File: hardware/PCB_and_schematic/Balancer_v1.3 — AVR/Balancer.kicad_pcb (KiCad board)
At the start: 2 copper layers, 99.5 x 99.5 mm, 218 parts, among them J1 External Current Shunt, J10 BATT_12V, J11 LOAD_RESISTOR, J12 V_MEAS, J13 LED, J14 ICP, J15 RS485, J16 RS485, J17 Conn_01x01, J2 BATT_IN, J3 BATT_OUT, J4 TMP_BALANCER, J5 TMP_SMPS, J6 THERMISTOR_BATT, J7 LOAD_RESISTOR, J8 FAN_BALANCER, J9 FAN_SMPS, Q1 IRF540N, Q10 BC817, Q11 BC807, Q12 IRF540N, Q13 BC817, Q14 BC817, Q15 AO3400A, Q16 AO3400A, Q17 BC817, Q18 BC817, Q19 BC807, Q20 IRF540N, Q21 BC817, Q5 IRF4905, Q6 BC817, Q7 BC807, Q8 BC817, Q9 BC817, U1 74AHCT125, U10 B0505S-1W, U11 ST485, U12 INA226, U13 FAN7382, U14 NE555D, U2 LM324, U3 LMV358, U4 AVR64DD28, U5 LM317_TO-220, U6 LM7805_TO220, U7 TL432DBZ, U8 ADUM3211ARZ, U9 PC817

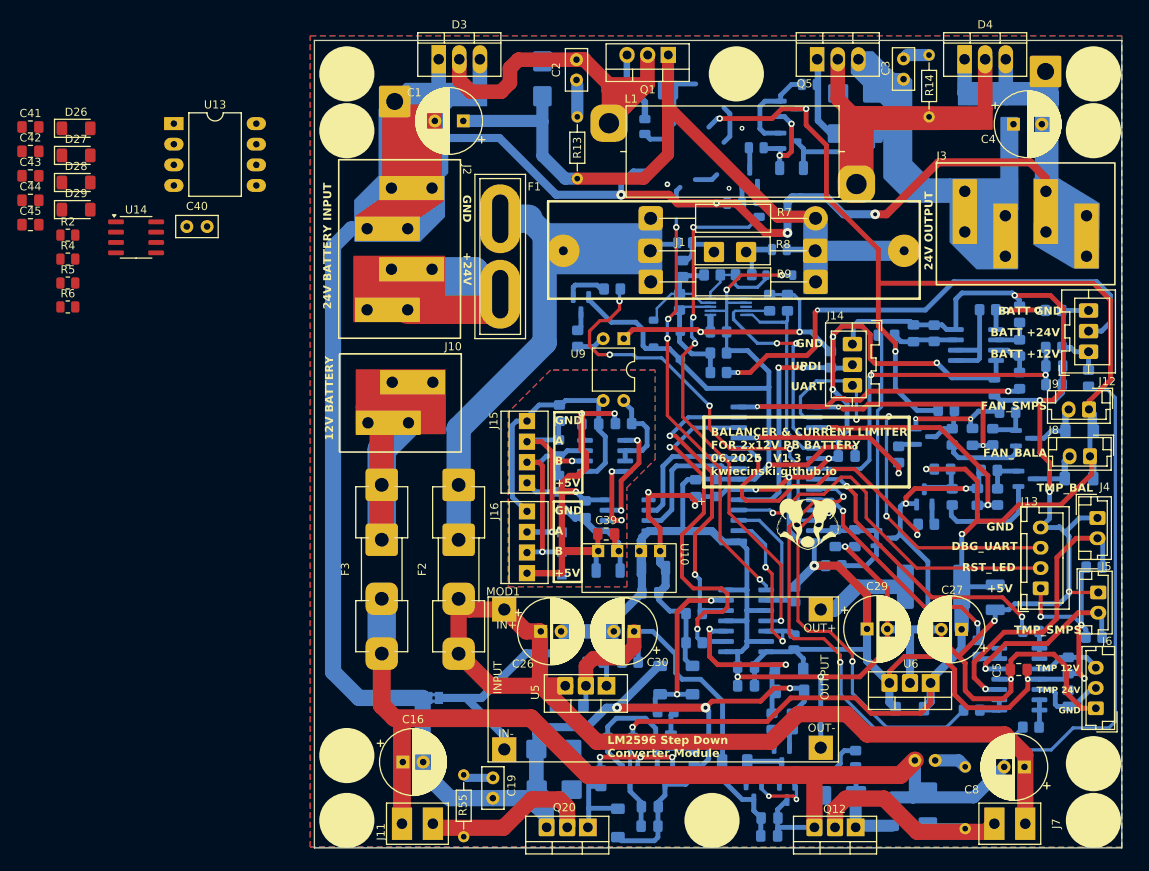
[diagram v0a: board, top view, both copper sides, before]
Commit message: add bms pcb balacer and smps separated
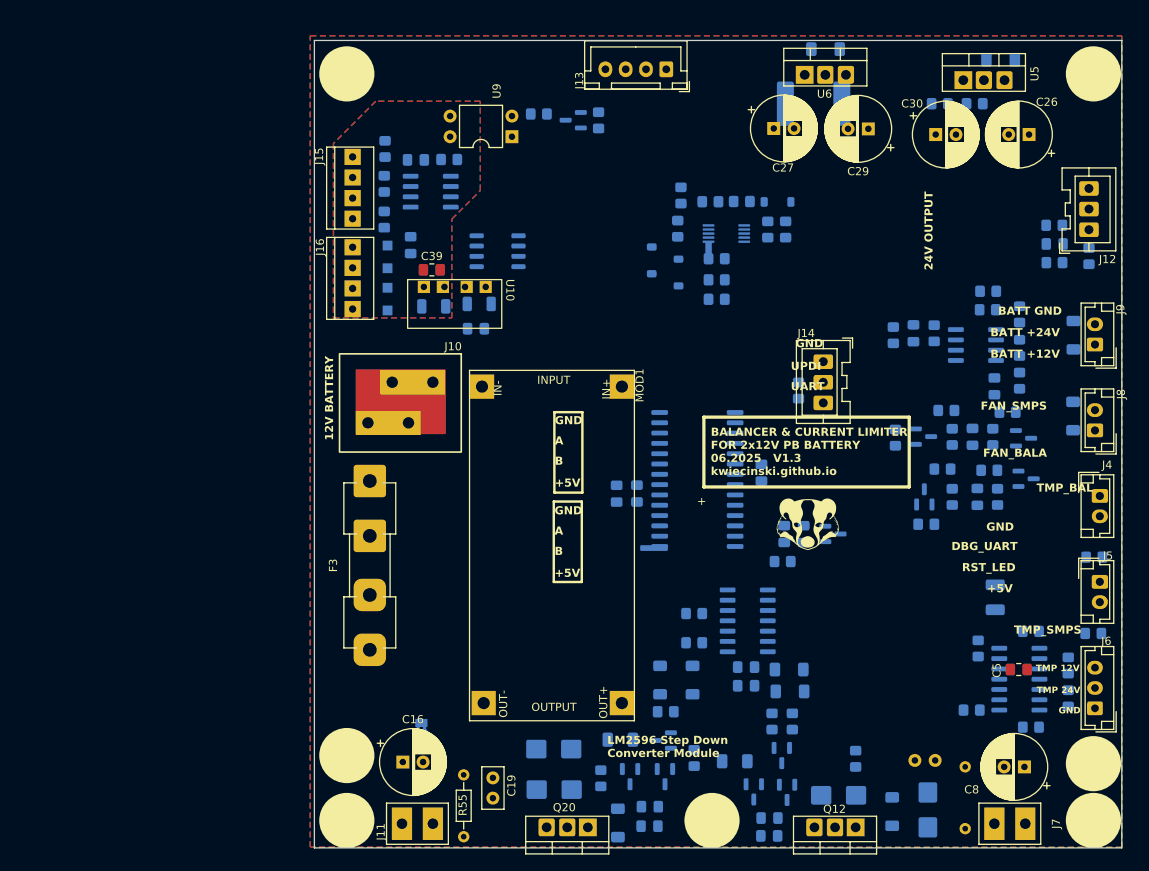
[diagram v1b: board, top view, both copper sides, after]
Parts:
- removed C1, C4: 100u/35V, Capacitor_THT:CP_Radial_D8.0mm_P3.50mm
- removed C2, C3: 1u, Capacitor_THT:C_Disc_D5.0mm_W2.5mm_P2.50mm
- removed C40: 100n, Capacitor_THT:C_Disc_D5.0mm_W2.5mm_P2.50mm
- removed C41, C42: 100n, Capacitor_SMD:C_0805_2012Metric_Pad1.18x1.45mm_HandSolder
- removed C43, C45: 10n, Capacitor_SMD:C_0805_2012Metric_Pad1.18x1.45mm_HandSolder
- removed C44: 1n, Capacitor_SMD:C_0805_2012Metric_Pad1.18x1.45mm_HandSolder
- removed D1, D2, D5, D6: SM6T15A, Diode_SMD:D_SMB
- removed D26, D28, D29: LL4148, Diode_SMD:D_MiniMELF
- removed D27: BZV55B15, Diode_SMD:D_MiniMELF
- removed D3, D4: YM3045, My-Footprints:TO-220-3_V_Thick_Pads
- removed F1: 6,3A, My-Footprints:Fuse_Blade_ATO_directSolder
- removed F2: 2A, My-Footprints:Fuseholder_Clip-5x20mm_Eaton_1A5601-01_Inline_P20.80x6.76mm_D1.70mm_Horizontal
- removed H2, H6, H8: MountingHole, My-Footprints:Mount-Hole-3mm
- removed J1: External Current Shunt, Connector_Hirose:Hirose_DF63M-2P-3.96DSA_1x02_P3.96mm_Vertical
- removed J17: Conn_01x01, Connector_Wire:SolderWire-1.5sqmm_1x01_D1.7mm_OD3.9mm
- removed J18: ~, Connector_Wire:SolderWire-1.5sqmm_1x01_D1.7mm_OD3.9mm
- removed J2: BATT_IN, My-Footprints-connectors:Flat-6,3mm-connector-4P
- removed J3: BATT_OUT, My-Footprints-connectors:Flat-6,3mm-connector-4P
- removed L1: L, My-Footprints:Inductor_Toroidal
- removed Q1: IRF540N, Package_TO_SOT_THT:TO-220-3_Vertical
- removed Q5: IRF4905, My-Footprints:TO-220-3_V_Thick_Pads
- removed Q6, Q8: BC817, Package_TO_SOT_SMD:SOT-23
- removed Q7: BC807, Package_TO_SOT_SMD:SOT-23
- removed R1, R2, R20: 10k, Resistor_SMD:R_0805_2012Metric
- removed R10: 20A/75mV, My-Footprints:Resistor-Power-5W-L22-W10
- removed R11, R3: 0R, Resistor_SMD:R_0805_2012Metric
- removed R12, R15, R4: 10R, Resistor_SMD:R_0805_2012Metric
- removed R13, R14: 10R, Resistor_THT:R_Axial_DIN0204_L3.6mm_D1.6mm_P7.62mm_Horizontal
- removed R16: 10k, Resistor_SMD:R_1206_3216Metric
- removed R17, R19, R5: 1k, Resistor_SMD:R_0805_2012Metric
- removed R18: 100R, Resistor_SMD:R_0805_2012Metric
- removed R6: 100k, Resistor_SMD:R_0805_2012Metric
- removed R7, R8, R9: 20A/75mV, Resistor_THT:R_Axial_DIN0309_L9.0mm_D3.2mm_P20.32mm_Horizontal
- removed U13: FAN7382, Package_DIP:DIP-8_W10.16mm_LongPads
- removed U14: NE555D, Package_SO:SOIC-8_3.9x4.9mm_P1.27mm
- moved D19 95.7 mm to (241.6, 53.3), turned to 180 degrees
- moved U5 86.6 mm to (237.0, 55.8), turned to 0 degrees
- moved C26 85.8 mm to (245.1, 62.5), turned to 180 degrees
- moved R64 83.2 mm to (238.4, 58.7), turned to 0 degrees
- moved D20 81.9 mm to (220.0, 52.0), turned to 0 degrees
- moved J13 78.9 mm to (200.4, 54.4), turned to 180 degrees
- moved R62 78.7 mm to (234.1, 58.7), turned to 180 degrees
- moved U6 76.5 mm to (217.4, 55.1), turned to 0 degrees
- moved C30 71.6 mm to (233.6, 62.5), turned to 0 degrees
- moved C27 65.9 mm to (213.6, 61.7), turned to 0 degrees
- moved C29 61.6 mm to (225.3, 61.8), turned to 180 degrees
- moved F4 61.3 mm to (218.5, 58.7), turned to 180 degrees
- moved MOD1 48.3 mm to (176.1, 91.5), turned to 0 degrees
- moved C31 39.0 mm to (177.3, 83.3)
- moved C33 39.0 mm to (169.5, 65.6)
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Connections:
- U1 pad 11: Net-(R19-Pad1) -> (no net)
- U1 pad 12: PWM_OUT_CHRG -> (no net)
- U1 pad 13: GND -> (no net)
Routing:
- net GND: track 477.0 -> 0.00 mm, vias 20 -> 0
- net GNDA: track 350.8 -> 0.00 mm, vias 7 -> 0
- net +5V: track 263.3 -> 0.00 mm, vias 15 -> 0
- net +12V_LOCAL: track 233.1 -> 0.00 mm, vias 6 -> 0
- net +BATT_12V: track 200.7 -> 0.00 mm
- net +BATT_24V: track 127.6 -> 0.00 mm
- net Net-(D1-A1): track 98.1 -> 0.00 mm
- net Net-(D2-A2): track 70.6 -> 0.00 mm
- net Net-(J2-Pin_3): track 66.2 -> 0.00 mm
- net Net-(R19-Pad1): track 64.8 -> 0.00 mm, vias 4 -> 0
- net DC_LINE_24V: track 62.9 -> 0.00 mm
- net Net-(F1-Pad2): track 62.6 -> 0.00 mm
- net TEMP_AKU_24V: track 62.5 -> 0.00 mm, vias 2 -> 0
- net VOLTAGE_BATT_24V_3W: track 61.6 -> 0.00 mm, vias 2 -> 0
- net (no net): track 61.3 -> 0.00 mm, vias 4 -> 0
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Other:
- board text removed: "+24V"
- board text removed: "24V BATTERY INPUT"

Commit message: routing power module
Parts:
- added J1: batt-24V-balancer, Connector_PinSocket_2.54mm:PinSocket_1x04_P2.54mm_Vertical, F.Cu at (189.9, 63.1)
- added J2: pwm-12v-local, Connector_PinSocket_2.54mm:PinSocket_1x04_P2.54mm_Vertical, F.Cu at (194.5, 63.1)
- added J3: R-Shunt, Connector_PinHeader_2.54mm:PinHeader_1x02_P2.54mm_Vertical, F.Cu at (199.1, 63.1)
- C39: moved to B.Cu
- moved F4 79.3 mm to (187.4, 131.6)
- moved R65 8.02 mm to (184.7, 64.0), turned to 0 degrees
- moved D20 7.05 mm to (219.8, 59.0)
- moved J13 6.00 mm to (206.3, 55.3)
- moved D19 5.26 mm to (241.0, 58.5)
- moved C32 4.93 mm to (181.5, 84.6)
- moved C39 4.81 mm to (175.2, 82.2)
- moved Q21 4.40 mm to (184.5, 60.7), turned to 90 degrees
- moved C31 3.91 mm to (181.0, 82.2)
- moved U10 3.77 mm to (172.1, 79.1)
- moved D12 3.44 mm to (250.3, 93.7)
- moved D13 3.44 mm to (250.3, 83.8)
- moved J12 3.44 mm to (252.3, 70.8)
- moved J4 3.44 mm to (253.6, 103.6)
- moved J5 3.44 mm to (253.6, 114.2)
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
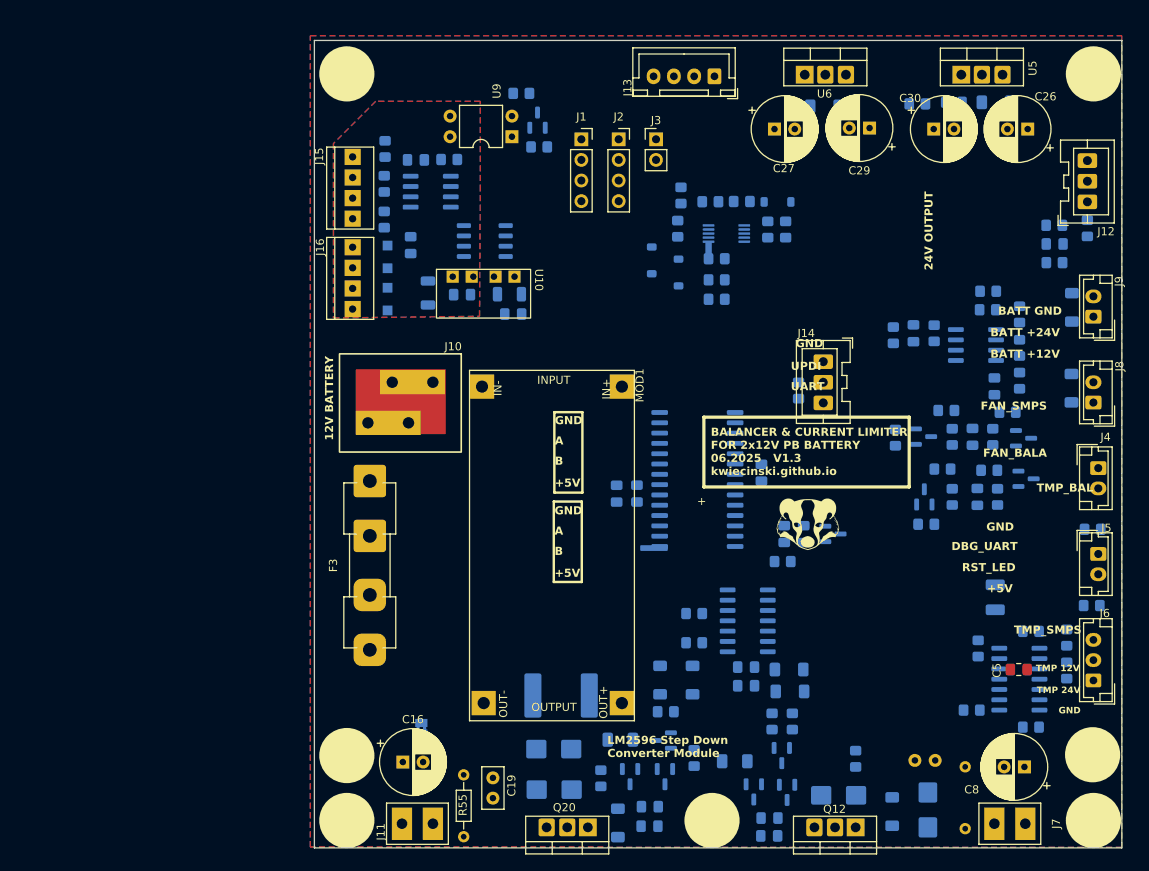
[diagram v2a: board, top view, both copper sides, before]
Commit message: done PCB power module and balancer
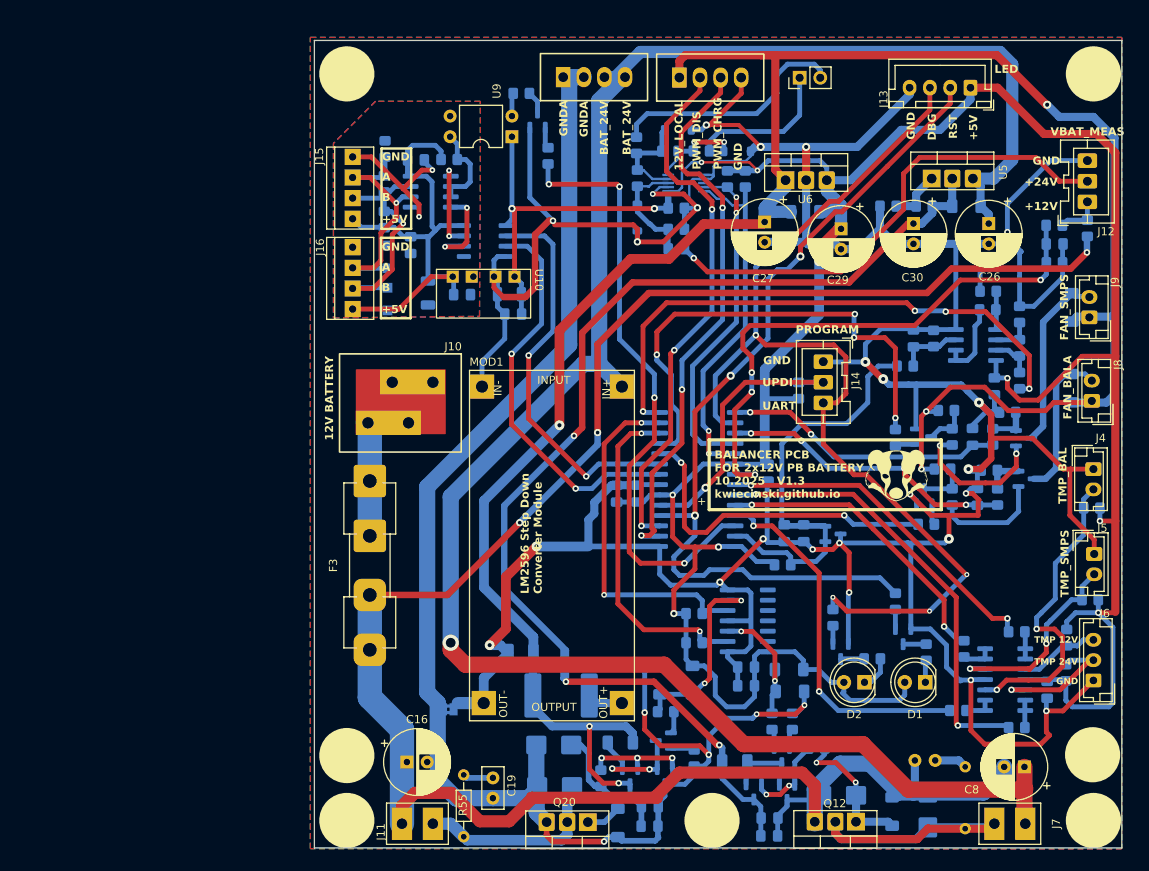
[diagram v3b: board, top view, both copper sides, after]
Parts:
- added D1: LED, LED_THT:LED_D5.0mm, F.Cu at (232.3, 130.0)
- added D2: LED, LED_THT:LED_D5.0mm, F.Cu at (224.8, 130.0)
- added Q1: BC817, Package_TO_SOT_SMD:SOT-23, B.Cu at (229.6, 124.3)
- added Q2: BC817, Package_TO_SOT_SMD:SOT-23, B.Cu at (221.8, 126.2)
- added R1: 10K, Resistor_SMD:R_0805_2012Metric_Pad1.20x1.40mm_HandSolder, B.Cu at (228.6, 120.0)
- added R2: 220R, Resistor_SMD:R_0805_2012Metric_Pad1.20x1.40mm_HandSolder, B.Cu at (232.4, 126.3)
- added R3: 10K, Resistor_SMD:R_0805_2012Metric_Pad1.20x1.40mm_HandSolder, B.Cu at (220.9, 122.0)
- added R4: 220R, Resistor_SMD:R_0805_2012Metric_Pad1.20x1.40mm_HandSolder, B.Cu at (225.8, 127.1)
- C5: moved to B.Cu
- J2: footprint Connector_PinSocket_2.54mm:PinSocket_1x04_P2.54mm_Vertical -> My-Footprints-connectors:PinSocket_1x04_P2.54mm_Vertical
- moved C24 58.9 mm to (182.5, 126.4), turned to 180 degrees
- moved J13 31.6 mm to (237.8, 56.7)
- moved J3 19.3 mm to (216.8, 55.5), turned to 90 degrees
- moved D24 16.4 mm to (201.8, 61.9), turned to 0 degrees
- moved U5 13.3 mm to (233.1, 67.9)
- moved D19 13.3 mm to (237.3, 71.3)
- moved R64 13.3 mm to (232.2, 71.3)
- moved D20 13.2 mm to (217.5, 72.0)
- moved U6 13.2 mm to (215.1, 68.1)
- moved R62 13.1 mm to (227.7, 71.3)
- moved C29 12.9 mm to (221.9, 74.1), turned to -90 degrees
- moved C26 12.6 mm to (240.1, 73.4), turned to -90 degrees
- moved G*** 12.4 mm to (228.7, 104.5)
- moved C30 11.9 mm to (230.8, 73.4), turned to -90 degrees
- moved C27 11.5 mm to (212.5, 73.2), turned to -90 degrees
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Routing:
- net GND: track 0.00 -> 526.2 mm, vias 0 -> 23
- net +5V: track 0.00 -> 383.5 mm, vias 0 -> 11
- net +12V_LOCAL: track 0.00 -> 288.6 mm, vias 0 -> 6
- net +BATT_12V: track 0.00 -> 258.3 mm, vias 0 -> 3
- net +BATT_24V: track 0.00 -> 254.3 mm, vias 0 -> 1
- net GNDA: track 0.00 -> 190.9 mm, vias 0 -> 5
- net +24V_LOCAL: track 0.00 -> 156.9 mm, vias 0 -> 3
- net DBG_UART: track 0.00 -> 125.4 mm, vias 0 -> 5
- net LED1_PF6_RST: track 0.00 -> 108.1 mm, vias 0 -> 3
- net RS485_OUTPUT_ENABLE: track 0.00 -> 75.0 mm, vias 0 -> 4
- net VOLTAGE_BATT_12V: track 0.00 -> 70.1 mm, vias 0 -> 4
- net GND_VOLTAGE_DROP_ADC: track 0.00 -> 69.4 mm, vias 0 -> 4
- net PWM_OUT_CHRG: track 0.00 -> 68.7 mm, vias 0 -> 3
- net PWM_OUT_DISCH: track 0.00 -> 66.2 mm, vias 0 -> 3
- net PWM_FAN_SMPS: track 0.00 -> 60.9 mm, vias 0 -> 4
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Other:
- board text added: "+12V"
- board text added: "+24V"
- board text added: "12V_LOCAL"
- board text added: "BALANCER PCB FOR 2x12V PB BATTERY 10.2025 V1.3 kwiecinski.github.io"
- board text added: "BAT_24V"
- board text added: "DBG"
- board text added: "GNDA"
- board text added: "LED"
- board text added: "PROGRAM"
- board text added: "PWM_CHRG"
- board text added: "PWM_DIS"
- board text added: "RST"
- board text added: "VBAT_MEAS"
- board text removed: "24V OUTPUT"
- board text removed: "BALANCER & CURRENT LIMITER FOR 2x12V PB BATTERY 06.2025 V1.3 kwiecinski.github.io"
- board text removed: "BATT +12V"
- board text removed: "BATT +24V"
- board text removed: "BATT GND"
- board text removed: "DBG_UART"
- board text removed: "RST_LED"
